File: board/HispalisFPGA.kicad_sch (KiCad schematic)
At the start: 80 parts, among them J1 Conn_02x03_Odd_Even, J2 Micro_SD_Card_Det_Hirose_DM3AT, J3 USBC, J4 Conn_01x24, J5 Conn_01x24, J6 Conn_02x09_Odd_Even, J7 Conn_01x06, SW1 SW_Push, U1 LFE5UM-285, U10 PUSB3FR4Z, U11 PUSB3FR4Z, U2 S27KS0641DPBHI020, U3 DSC6001CI2A-016.0000T, U4 FAN53555, U5 MIC5504-2.5YMT-TR, U6 Conn_02x03_Counter_Clockwise, U7 FAN53600, U8 S25FL064L, U9 MIC5504-1.2YMT-TR

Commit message: Add PMODs, LEDs, switches and buttons
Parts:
- removed C1: 1uF, Footprints:C_0402_NoSilk, symbol Device:C_Small
- removed C2: 100nF, Footprints:C_0402_NoSilk, symbol Device:C_Small
- removed C33: 10uF, Footprints:C_0402_NoSilk, symbol Device:C_Small
- removed J2: Micro_SD_Card_Det_Hirose_DM3AT, Footprints:DM3D-SF, symbol HispalisFPGA-rescue:Micro_SD_Card_Det_Hirose_DM3AT-Connector
- removed J4, J5: Conn_01x24, Pin_Headers:Pin_Header_Straight_1x24_Pitch2.54mm, symbol Connector_Generic:Conn_01x24
- removed J6: Conn_02x09_Odd_Even, symbol Connector_Generic:Conn_02x11_Odd_Even
- removed R6: 100K, Footprints:R_0402_NoSilk, symbol Device:R_Small
- added BTNC, BTND, BTNL, BTNR, BTNU: SW_Push, Button_Switch_THT:SW_PUSH_6mm, symbol Switch:SW_Push
- added L1, L2, L3, L4, L5, L6, L7, L8: LED, LED_SMD:LED_0805_2012Metric, symbol Device:LED
- added PMOD1: Conn_02x06_Top_Bottom, Connector_PinSocket_2.54mm:PinSocket_2x06_P2.54mm_Horizontal, symbol Connector_Generic:Conn_02x06_Top_Bottom
- added PMOD2, PMOD3, PMOD4: Conn_02x06_Top_Bottom, symbol Connector_Generic:Conn_02x06_Top_Bottom
- added R1, R14, R15, R16, R17, R18, R19, R2, R20, R21, R22, R6, R9: 10K, Resistor_SMD:R_0402_1005Metric, symbol Device:R
- added R23, R24, R25, R26, R27, R28, R29, R30: 200R, Resistor_SMD:R_0402_1005Metric, symbol Device:R
- added SW2: SW_DIP_x08, Button_Switch_SMD:SW_DIP_SPSTx04_Slide_6.7x11.72mm_W6.73mm_P2.54mm_LowProfile_JPin, symbol Switch:SW_DIP_x08
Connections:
- net +3V3: now also BTNC.2, BTND.2, BTNL.2, BTNR.2, BTNU.2, PMOD1.12 (Pin_12), PMOD1.6 (Pin_6), PMOD2.12 (Pin_12), PMOD2.6 (Pin_6), PMOD3.12 (Pin_12), PMOD3.6 (Pin_6), PMOD4.12 (Pin_12), PMOD4.6 (Pin_6), SW2.10, SW2.11, SW2.12, SW2.13, SW2.14, SW2.15, SW2.16, SW2.9
- net GND: now also PMOD1.11 (Pin_11), PMOD1.5 (Pin_5), PMOD2.11 (Pin_11), PMOD2.5 (Pin_5), PMOD3.11 (Pin_11), PMOD3.5 (Pin_5), PMOD4.11 (Pin_11), PMOD4.5 (Pin_5), R1.2, R14.2, R15.2, R16.2, R17.2, R18.2, R19.2, R2.2, R20.2, R21.2, R22.2, R23.2, R24.2, R25.2, R26.2, R27.2, R28.2, R29.2, R30.2, R6.2, R9.2
- net PIN48: no longer U1.A7 (PR8AB-/RDQSN8)
- net PIN1 renamed PMOD1_1
- net PMOD1_1: now also PMOD1.1 (Pin_1)
- net PIN10 renamed PMOD2_2
- net PMOD2_2: now also PMOD2.2 (Pin_2)
- net PIN11 renamed PMOD2_3
- net PMOD2_3: now also PMOD2.3 (Pin_3)
- net PIN12 renamed PMOD2_4
- net PMOD2_4: now also PMOD2.4 (Pin_4)
- net PIN13 renamed PMOD2_7
- net PMOD2_7: now also PMOD2.7 (Pin_7)
- net PIN14 renamed PMOD2_8
- net PMOD2_8: now also PMOD2.8 (Pin_8)
- net PIN15 renamed PMOD2_9
- net PMOD2_9: now also PMOD2.9 (Pin_9)
- net PIN16 renamed PMOD2_10
- net PMOD2_10: now also PMOD2.10 (Pin_10)
- net PIN17 renamed PMOD3_1
- net PMOD3_1: now also PMOD3.1 (Pin_1)
- net PIN18 renamed PMOD3_2
- net PMOD3_2: now also PMOD3.2 (Pin_2)
- net PIN19 renamed PMOD3_3
- net PMOD3_3: now also PMOD3.3 (Pin_3)
- net PIN2 renamed PMOD1_2
- net PMOD1_2: now also PMOD1.2 (Pin_2)
- net PIN20 renamed PMOD3_4
- net PMOD3_4: now also PMOD3.4 (Pin_4)
- net PIN21 renamed PMOD3_7
- net PMOD3_7: now also PMOD3.7 (Pin_7)
- net PIN22 renamed PMOD3_8
- net PMOD3_8: now also PMOD3.8 (Pin_8)
- net PIN23 renamed PMOD3_9
- net PMOD3_9: now also PMOD3.9 (Pin_9)
- net PIN24 renamed PMOD3_10
- net PMOD3_10: now also PMOD3.10 (Pin_10)
- net PIN25 renamed PMOD4_1
- net PMOD4_1: now also PMOD4.1 (Pin_1)
- net PIN26 renamed PMOD4_2
- net PMOD4_2: now also PMOD4.2 (Pin_2)
- net PIN27 renamed PMOD4_3
- net PMOD4_3: now also PMOD4.3 (Pin_3)
- net PIN28 renamed PMOD4_4
- net PMOD4_4: now also PMOD4.4 (Pin_4)
- net PIN29 renamed PMOD4_7
- net PMOD4_7: now also PMOD4.7 (Pin_7)
- net PIN3 renamed PMOD1_3
- net PMOD1_3: now also PMOD1.3 (Pin_3)
- net PIN30 renamed PMOD4_8
- net PMOD4_8: now also PMOD4.8 (Pin_8)
- net PIN31 renamed PMOD4_9
- net PMOD4_9: now also PMOD4.9 (Pin_9)
- net PIN32 renamed PMOD4_10
- net PMOD4_10: now also PMOD4.10 (Pin_10)
- net PIN33 renamed LED1
- net LED1: now also L1.1 (K)
- net PIN34 renamed LED2
- net LED2: now also L2.1 (K)
- net PIN35 renamed LED3
- net LED3: now also L3.1 (K)
- net PIN36 renamed LED4
- net LED4: now also L4.1 (K)
- net PIN37 renamed LED5
- net LED5: now also L5.1 (K)
- net PIN38 renamed LED6
- net LED6: now also L6.1 (K)
- net PIN39 renamed LED7
- net LED7: now also L7.1 (K)
- net PIN4 renamed PMOD1_4
- net PMOD1_4: now also PMOD1.4 (Pin_4)
- net PIN40 renamed LED8
- net LED8: now also L8.1 (K)
- net PIN41 renamed SW1
- net SW1: now also R15.1, SW2.1
- net PIN42 renamed SW2
- net SW2: now also R16.1, SW2.2
- net PIN43 renamed SW3
- net SW3: now also R17.1, SW2.3
- net PIN44 renamed SW4
- net SW4: now also R18.1, SW2.4
- net PIN45 renamed SW5
- net SW5: now also R19.1, SW2.5
- net PIN46 renamed SW6
- net SW6: now also R20.1, SW2.6
- net PIN47 renamed SW7
- net SW7: now also R21.1, SW2.7
- net PIN49 renamed BTN1
- net BTN1: now also BTND.1, R1.1
- net PIN5 renamed PMOD1_7
- net PMOD1_7: now also PMOD1.7 (Pin_7)
- net PIN50 renamed BTN2
- net BTN2: now also BTNR.1, R2.1
- net PIN51 renamed BTN3
- net BTN3: now also BTNL.1, R6.1
- net PIN52 renamed BTN4
- net BTN4: now also BTNU.1, R9.1
- net PIN53 renamed BTN5
- net BTN5: now also BTNC.1, R14.1
- net PIN6 renamed PMOD1_8
- net PMOD1_8: now also PMOD1.8 (Pin_8)
- net PIN7 renamed PMOD1_9
- net PMOD1_9: now also PMOD1.9 (Pin_9)
- net PIN8 renamed PMOD1_10
- net PMOD1_10: now also PMOD1.10 (Pin_10)
- net PIN9 renamed PMOD2_1
- net PMOD2_1: now also PMOD2.1 (Pin_1)
- net SDCARD_CLK: no longer names the net of U1.B10 (PT29AB+/PCLKT0_0)
- net SDCARD_CMD: no longer names the net of U1.A4 (PR11AB-)
- net SDCARD_DAT0: no longer names the net of U1.A10 (PT27AB-/PCLKC0_1)
- net SDCARD_DAT1: no longer names the net of U1.A9 (PT35AB+/PCLKT1_0)
- net SDCARD_DAT2: no longer names the net of U1.A8 (PT35AB-/PCLKC1_0)
- net SDCARD_DAT3_CD: no longer names the net of U1.D4 (PR14AB+)
- net SDCARD_DET: no longer names the net of U1.B9 (PT33AB+/PCLKT1_1)
- new net: L8.2 (A), R30.1
- new net: L4.2 (A), R26.1
- new net: L1.2 (A), R23.1
- new net: L7.2 (A), R29.1
- new net: L5.2 (A), R27.1
- new net: L2.2 (A), R24.1
- new net: L6.2 (A), R28.1
- new net: L3.2 (A), R25.1
- new net SW8: R22.1, SW2.8, U1.A7 (PR8AB-/RDQSN8)
- no-connect marks 0 -> 1
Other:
- note added: "I/O Devices"
- note removed: "Bottom Header"
- note removed: "Micro SD Card Slot"

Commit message: Add 7-segment 4-digit display and annotate components
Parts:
- added R31, R32, R33, R34, R35, R36, R37, R38: 500R, symbol Device:R
- added U12: LTC-4627JR, Display_7Segment:LTC-4627Jx, symbol Display_Character:LTC-4627JR
- renumbered BTND to BTN1, BTNR to BTN2, BTNL to BTN3, BTNU to BTN4, BTNC to BTN5, L1 to LD1, L2 to LD2, L3 to LD3, L4 to LD4, L5 to LD5, L6 to LD6, L7 to LD7, L8 to LD8
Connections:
- net +1V1: no longer U1.C10 (PT29AB-/PCLKC0_0), U1.C11 (PT4AB-), U1.C8 (PT67AB-), U1.C9 (PT33AB-/PCLKC1_1), U1.J16 (PL35CD-), U1.J3 (PR29CD+/GR_PCLK3_1), U1.K15 (PL41CD-), U1.K16 (PL41CD+), U1.K3 (PR41CD+), U1.K4 (PR38AB+), U1.L15 (PL44CD+), U1.L16 (PL44CD-), U1.L3 (PR41AB-), U1.L4 (PR38AB-), U1.M16 (PL47CD+/LLC_GPLL0T_IN), U1.M3 (PR41AB+)
- net +3V3: no longer U1.C12 (PL2AB+), U1.C13 (PL8AB-/LDQSN8), U1.C6 (PR5AB-), U1.C7 (PR2AB+), U1.D13 (PL8AB+/LDQS8), U1.D6 (PR5AB+), U1.G15 (PL35AB+), U1.G4 (PR26AB-/PCLKC3_1), U1.H15 (PL35AB-), U1.H4 (PR26AB+/PCLKT3_1), U1.N15 (PB4AB+)
- new net: R31.2, U12.14 (A)
- new net: R32.2, U12.16 (B)
- new net: R35.2, U12.5 (E)
- new net: R36.2, U12.11 (F)
- new net: R34.2, U12.3 (D)
- new net: R33.2, U12.13 (C)
- new net: R37.2, U12.15 (G)
- new net: R38.2, U12.7 (DP)
- new net DISPLAY_A1: U12.1 (CA1)
- new net DISPLAY_A2: U12.2 (CA2)
- new net DISPLAY_A3: U12.6 (CA3)
- new net DISPLAY_A4: U12.8 (CA4)
- new net DISPLAY_AL: U12.4 (CAL)
- new net DISPLAY_CA: R31.1
- new net DISPLAY_CB: R32.1
- new net DISPLAY_CC: R33.1
- new net DISPLAY_CD: R34.1
- new net DISPLAY_CDP: R38.1
- new net DISPLAY_CE: R35.1
- new net DISPLAY_CF: R36.1
- new net DISPLAY_CG: R37.1
- no-connect marks 1 -> 2
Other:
- note added: "Display"

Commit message: Fix and adjust power connections
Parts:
- removed R3, R8: 0, Footprints:R_0402_NoSilk, symbol Device:R_Small
- U4: value FAN53555 -> FAN53555UC04X
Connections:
- net PIN48 is gone; now on net STATUS_LED: D2.2 (A)
- net GND: now also U4.A1 (VSEL)
- net STATUS_LED: now reaches U1.C12 (PL2AB+)
- net +1V2A renamed +1V2
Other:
- note added: "1.1 Volt Switching Regulator"
- note removed: "1.2 Volt Switching Regulator"
- note removed: "Place R3 for 1.2v operation Place R8 for 1.1v operation"

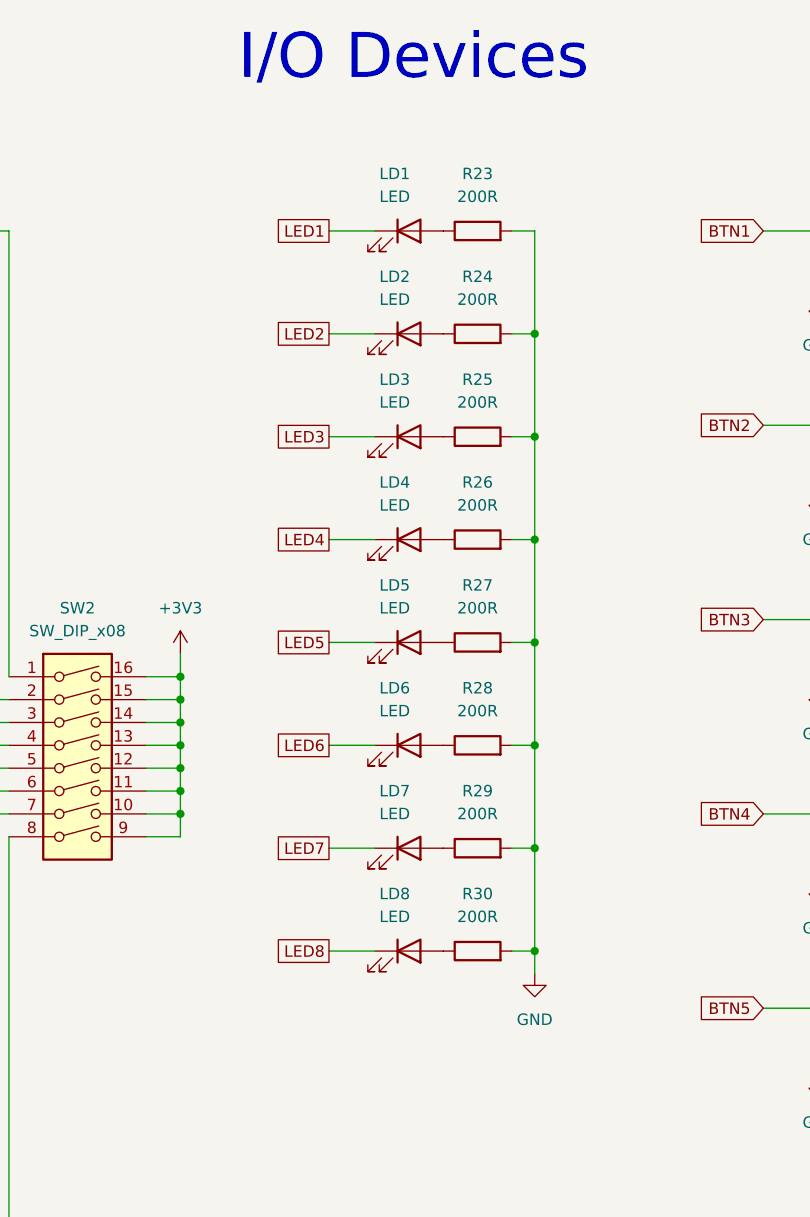
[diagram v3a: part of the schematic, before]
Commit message: Fix LEDs polarity
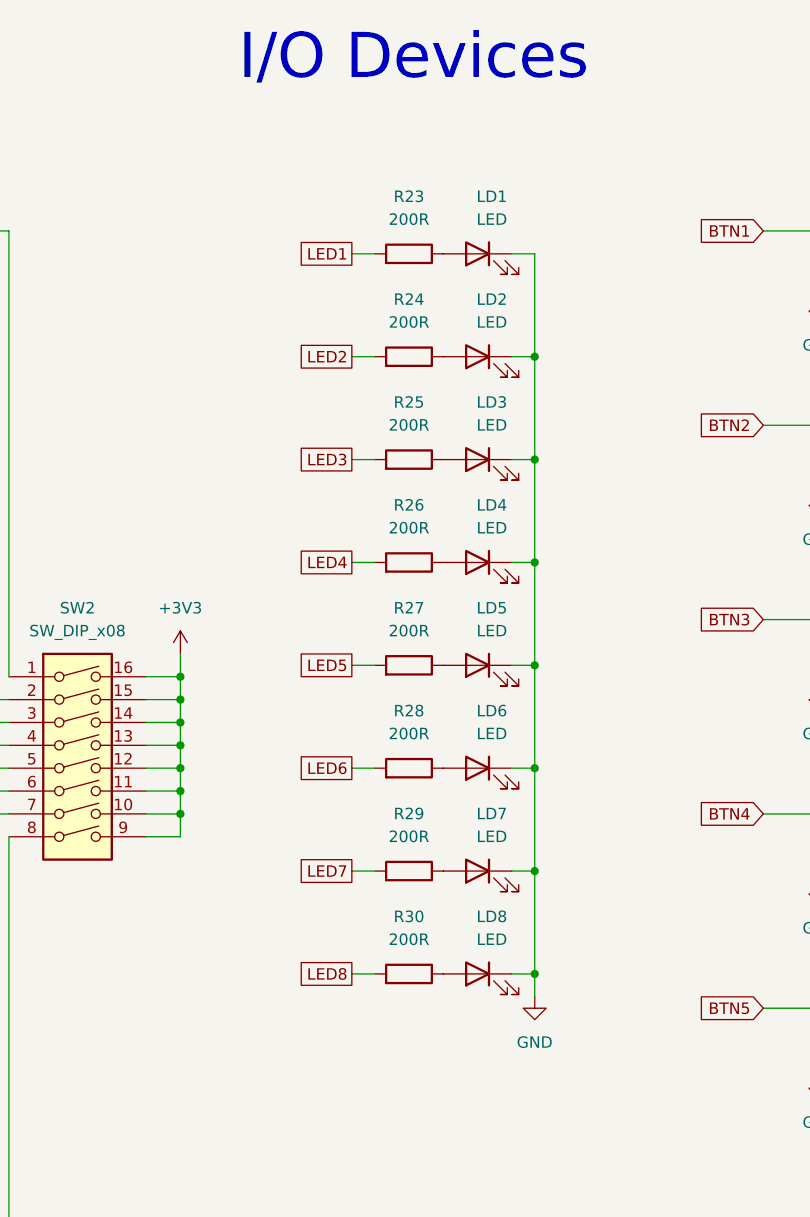
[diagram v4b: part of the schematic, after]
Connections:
- net GND: now also LD1.1 (K), LD2.1 (K), LD3.1 (K), LD4.1 (K), LD5.1 (K), LD6.1 (K), LD7.1 (K), LD8.1 (K); no longer R23.2, R24.2, R25.2, R26.2, R27.2, R28.2, R29.2, R30.2
- net LED1: now also R23.2; no longer LD1.1 (K)
- net LED2: now also R24.2; no longer LD2.1 (K)
- net LED3: now also R25.2; no longer LD3.1 (K)
- net LED4: now also R26.2; no longer LD4.1 (K)
- net LED5: now also R27.2; no longer LD5.1 (K)
- net LED6: now also R28.2; no longer LD6.1 (K)
- net LED7: now also R29.2; no longer LD7.1 (K)
- net LED8: now also R30.2; no longer LD8.1 (K)
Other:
- moved on the sheet: LD1, LD2, LD3, LD4, LD5, LD6, LD7, LD8, R23, R24, R25, R26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

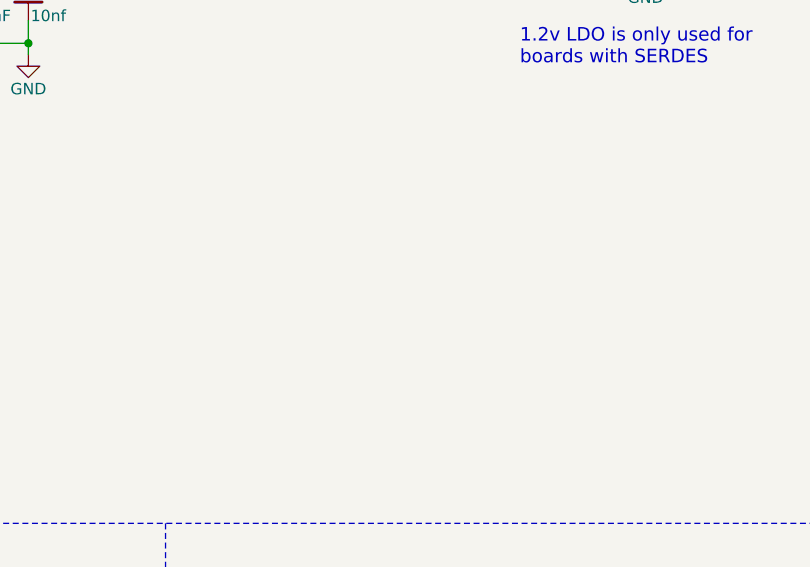
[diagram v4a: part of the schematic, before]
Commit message: Add socket wire for 5V power input-output
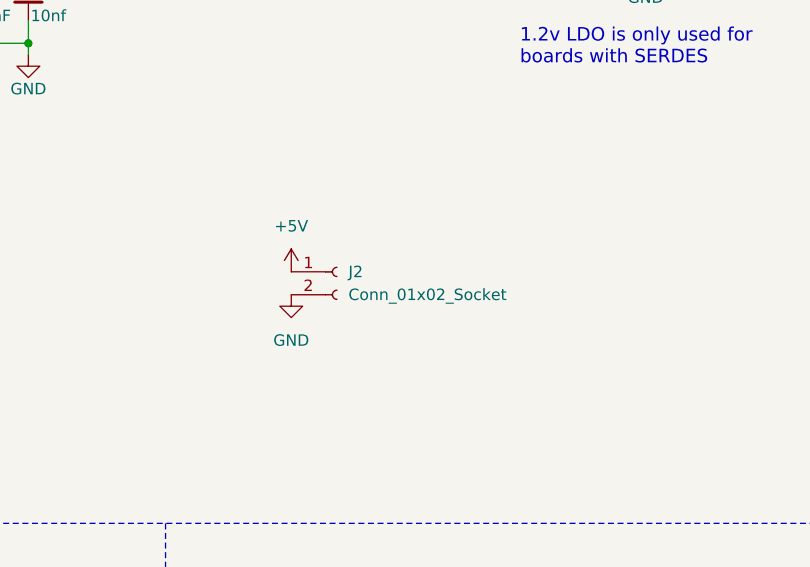
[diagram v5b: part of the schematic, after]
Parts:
- added J2: Conn_01x02_Socket, Connector_PinSocket_2.54mm:PinSocket_1x02_P2.54mm_Vertical, symbol Connector:Conn_01x02_Socket
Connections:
- net +5V: now also J2.1 (Pin_1)
- net GND: now also J2.2 (Pin_2)
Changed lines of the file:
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@@
+	(symbol
+		(lib_id "power:GND")
+		(at 119.38 271.78 0)
+		(unit 1)
+		(exclude_from_sim no)
+		(in_bom yes)
+		(on_board yes)
+		(dnp no)
+		(fields_autoplaced yes)
+		(property "Reference" "#PWR068"
+			(at 119.38 278.13 0)
+			(effects
+				(font
+					(size 1.27 1.27)
+				)
+				(hide yes)
+			)
+		)
+		(property "Value" "GND"
+			(at 119.38 276.86 0)
+			(effects
+				(font
+					(size 1.27 1.27)
+				)
+			)
+		)
+		(property "Footprint" ""
+			(at 119.38 271.78 0)
+			(effects
+				(font
+					(size 1.27 1.27)
+				)
+				(hide yes)
+			)
+		)
+		(property "Datasheet" ""
+			(at 119.38 271.78 0)
+			(effects
+				(font
+					(size 1.27 1.27)
+				)
+				(hide yes)
+			)
+		)
+		(property "Description" "Power symbol creates a global label with name \"GND\" , ground"
+			(at 119.38 271.78 0)
+			(effects
+				(font
+					(size 1.27 1.27)
+				)
+				(hide yes)
+			)
+		)
+		(pin "1"
+		)
+		(instances
+			(project "HispalisFPGA"
+				(path "/864346d0-d3ef-428e-a44f-9476f195db98"
+					(reference "#PWR068")
+					(unit 1)
+				)
+			)
+		)
+	)
 	(symbol
 		(lib_id "power:GND")
@@
 	)
 	(symbol
+		(lib_id "Connector:Conn_01x02_Socket")
+		(at 124.46 269.24 0)
+		(unit 1)
+		(exclude_from_sim no)
+		(in_bom yes)
+		(on_board yes)
+		(dnp no)
+		(fields_autoplaced yes)
+		(property "Reference" "J2"
+			(at 125.73 269.2399 0)
+			(effects
+				(font
+					(size 1.27 1.27)
+				)
+				(justify left)
+			)
+		)
+		(property "Value" "Conn_01x02_Socket"
+			(at 125.73 271.7799 0)
+			(effects
+				(font
+					(size 1.27 1.27)
+				)
+				(justify left)
+			)
+		)
+		(property "Footprint" "Connector_PinSocket_2.54mm:PinSocket_1x02_P2.54mm_Vertical"
+			(at 124.46 269.24 0)
+			(effects
+				(font
+					(size 1.27 1.27)
+				)
+				(hide yes)
+			)
+		)
+		(property "Datasheet" "~"
+			(at 124.46 269.24 0)
+			(effects
+				(font
+					(size 1.27 1.27)
+				)
+				(hide yes)
+			)
+		)
+		(property "Description" "Generic connector, single row, 01x02, script generated"
+			(at 124.46 269.24 0)
+			(effects
+				(font
+					(size 1.27 1.27)
+				)
+				(hide yes)
+			)
+		)
+		(pin "1"
+		)
+		(pin "2"
+		)
+		(instances
+			(project "HispalisFPGA"
+				(path "/864346d0-d3ef-428e-a44f-9476f195db98"
+					(reference "J2")
+					(unit 1)
+				)
+			)
+		)
+	)
+	(symbol
 		(lib_id "power:GND")
 		(at 214.63 265.43 0)
@@
 					(unit 1)
 				)
+			)
+		)
+	)
+	(symbol
+		(lib_id "power:+5V")
+		(at 119.38 269.24 0)
+		(unit 1)
+		(exclude_from_sim no)
+		(in_bom yes)
+		(on_board yes)
+		(dnp no)
+		(fields_autoplaced yes)
+		(property "Reference" "#PWR067"
+			(at 119.38 273.05 0)
+			(effects
+				(font
+					(size 1.27 1.27)
+				)
+				(hide yes)
+			)
+		)
+		(property "Value" "+5V"
+			(at 119.38 264.16 0)
+			(effects
+				(font
+					(size 1.27 1.27)
+				)
+			)
+		)
+		(property "Footprint" ""
+			(at 119.38 269.24 0)
+			(effects
+				(font
+					(size 1.27 1.27)
+				)
+				(hide yes)
+			)
+		)
+		(property "Datasheet" ""
+			(at 119.38 269.24 0)
+			(effects
+				(font
+					(size 1.27 1.27)
+				)
+				(hide yes)
+			)
+		)
+		(property "Description" "Power symbol creates a global label with name \"+5V\""
+			(at 119.38 269.24 0)
+			(effects
+				(font
+					(size 1.27 1.27)
+				)
+				(hide yes)
+			)
+		)
+		(pin "1"
+		)
+		(instances
+			(project "HispalisFPGA"
+				(path "/864346d0-d3ef-428e-a44f-9476f195db98"
+					(reference "#PWR067")
+					(unit 1)
+				)
